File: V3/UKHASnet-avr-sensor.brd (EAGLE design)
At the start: 49.5 x 49.2 mm, 25 parts, among them J1 AVR_SPI_PRG_62X3_LOCK, U1 MCP1700-3302E/TO, U2 ATMEGA328P-PU, X2 SMA-142-0711-821/826, Y1 RESONATORPTH

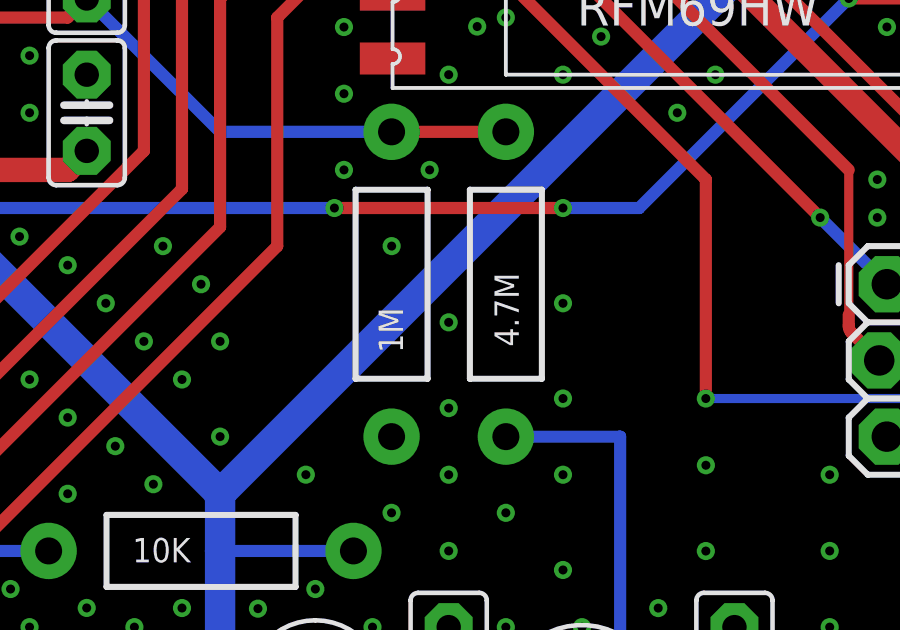
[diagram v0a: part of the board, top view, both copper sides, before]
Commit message: Reduce Battery Voltage Resistor Divider Values.
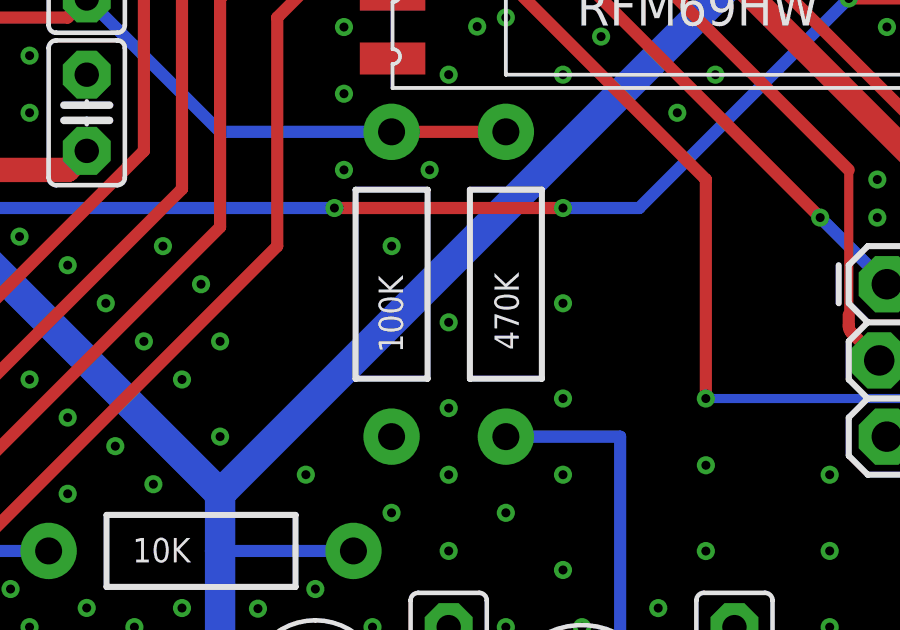
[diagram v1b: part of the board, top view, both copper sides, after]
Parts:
- R1: value 1M -> 100K
- R2: value 4.7M -> 470K
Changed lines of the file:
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@@
 </element>
 <element name="JP9" library="SparkFun-Connectors" package="1X01" value="M01PTH" x="24.765" y="46.355" smashed="yes"/>
-<element name="R1" library="SparkFun" package="AXIAL-0.4" value="1M" x="27.941" y="19.05" smashed="yes" rot="R90">
+<element name="R1" library="SparkFun" package="AXIAL-0.4" value="100K" x="27.941" y="19.05" smashed="yes" rot="R90">
 <attribute name="VALUE" x="28.322" y="16.764" size="0.8128" layer="21" font="vector" ratio="15" rot="R90"/>
 </element>
-<element name="R2" library="SparkFun" package="AXIAL-0.4" value="4.7M" x="31.751" y="19.05" smashed="yes" rot="R270">
+<element name="R2" library="SparkFun" package="AXIAL-0.4" value="470K" x="31.751" y="19.05" smashed="yes" rot="R270">
 <attribute name="VALUE" x="31.37" y="19.431" size="0.8128" layer="21" font="vector" ratio="15" rot="R270"/>
 </element>

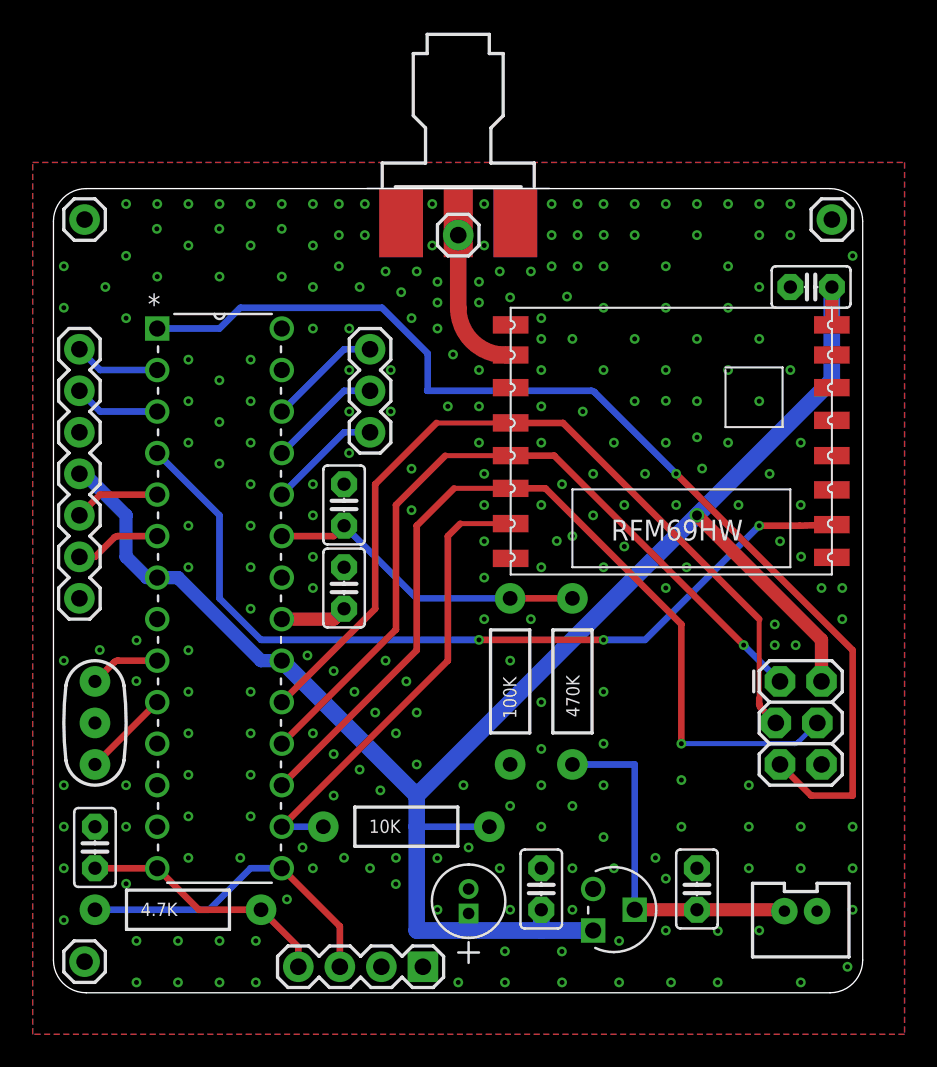
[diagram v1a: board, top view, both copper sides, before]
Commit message: Tweak component placement, add vias, more silk labels.
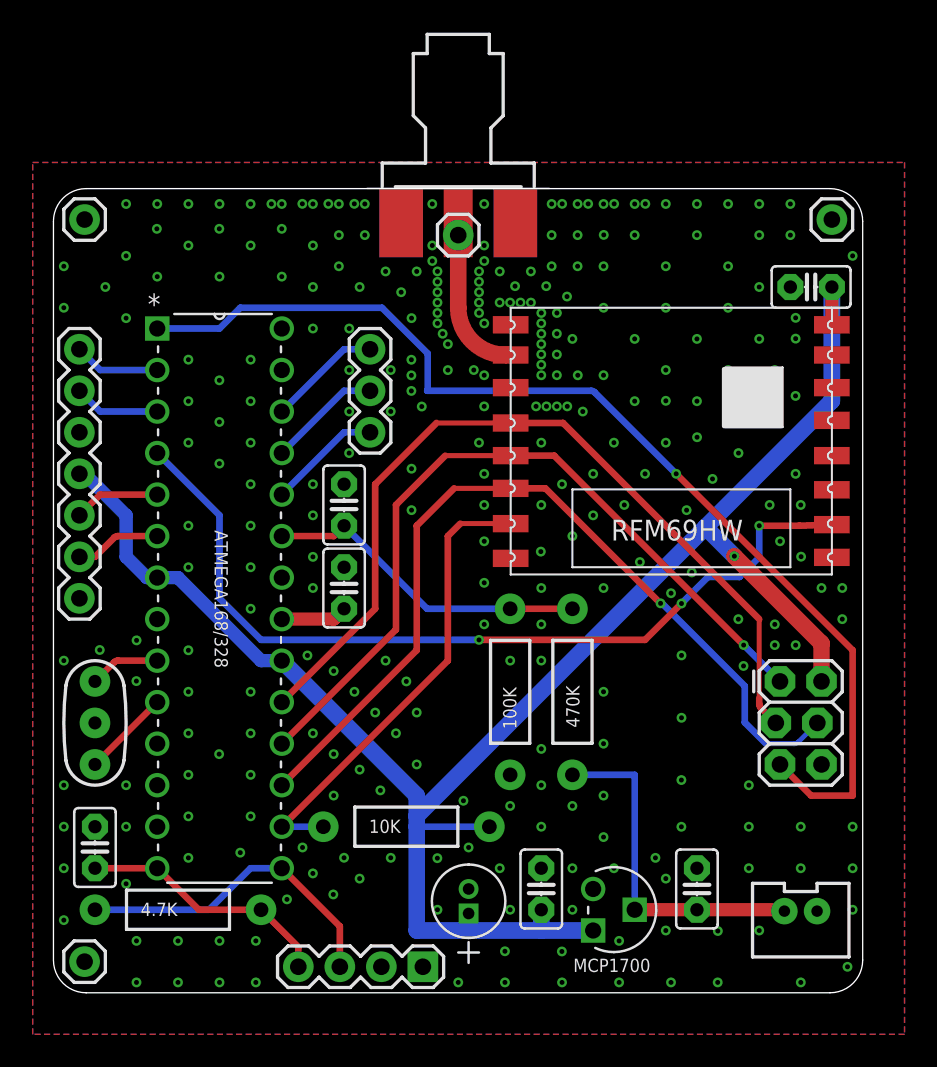
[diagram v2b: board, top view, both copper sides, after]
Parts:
- moved R1 0.64 mm to (27.9, 18.4)
- moved R2 0.64 mm to (31.8, 18.4)
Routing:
- net MOSI: track 56.0 -> 53.1 mm
- net INT0: track 51.9 -> 53.0 mm
- net VIN: track 21.9 -> 21.3 mm
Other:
- board text added: "ATMEGA168/328"
- board text added: "MCP1700"
